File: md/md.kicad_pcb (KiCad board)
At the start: 2 copper layers, 59.7 x 67.3 mm, 55 parts, among them J1 OutB, J2 OutA, J3 Interface, J4 12VJmp, J5 Conn_02x08_Counter_Clockwise, J6 Conn_02x08_Counter_Clockwise, J7 Conn_02x08_Counter_Clockwise, J8 Conn_02x08_Counter_Clockwise, Q1 FETA(IRFB7437PBF), Q2 FETA(IRFB7437PBF), Q3 FETB(IRFB7437PBF), Q4 FETB(IRFB7437PBF), U1 TLP2105, U2 IR7184S, U3 IR7184S, U4 7400, U5 L7812

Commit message: finished working
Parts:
- moved C4 7.62 mm to (179.1, 104.1)
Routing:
- net +24V: track 173.1 -> 174.3 mm
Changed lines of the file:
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@@
     (links 166)
     (no_connects 0)
-    (area 172.644999 50.146665 234.945 134.003335)
+    (area 172.644999 57.074999 232.485001 124.535001)
     (thickness 1.6)
     (drawings 12)
-    (tracks 485)
+    (tracks 488)
     (zones 0)
     (modules 55)
@@
   )
   (module Capacitors_THT:CP_Radial_D8.0mm_P5.00mm (layer F.Cu)
-    (at 179.07 111.76)
+    (at 179.07 104.14)
     (descr "CP, Radial series, Radial, pin pitch=5.00mm, , diameter=8mm, Electrolytic Capacitor")
     (tags "CP Radial series Radial pin pitch 5.00mm  diameter 8mm Electrolytic Capacitor")
@@
   (segment (start 230.505 86.36) (end 230.505 88.15) (width 0.25) (layer F.Cu) (net 2))
   (segment (start 230.505 88.15) (end 230.62 88.265) (width 0.25) (layer F.Cu) (net 2))
+  (segment (start 184.07 104.14) (end 184.07 103.979998) (width 0.25) (layer B.Cu) (net 3))
   (segment (start 189.484 94.488) (end 188.481998 94.488) (width 0.25) (layer F.Cu) (net 3))
   (segment (start 188.481998 94.488) (end 187.719998 95.25) (width 0.25) (layer F.Cu) (net 3))
@@
   (segment (start 212.49 82.37) (end 213.54 83.42) (width 0.6) (layer F.Cu) (net 9))
   (segment (start 213.54 83.42) (end 213.54 83.82) (width 0.6) (layer F.Cu) (net 9))
+  (segment (start 179.07 100.718002) (end 179.07 105.41) (width 2) (layer B.Cu) (net 10))
+  (segment (start 179.07 105.41) (end 179.07 108.96) (width 2) (layer B.Cu) (net 10))
+  (segment (start 179.07 104.14) (end 179.07 105.41) (width 0.25) (layer B.Cu) (net 10))
   (segment (start 213.36 91.96) (end 212.84 91.96) (width 0.6) (layer F.Cu) (net 10))
   (segment (start 212.84 91.96) (end 209.55 95.25) (width 0.6) (layer F.Cu) (net 10))
@@
   (segment (start 185.42 59.549998) (end 185.42 94.368002) (width 2) (layer B.Cu) (net 10))
   (segment (start 185.42 94.368002) (end 179.07 100.718002) (width 2) (layer B.Cu) (net 10))
-  (segment (start 179.07 100.718002) (end 179.07 108.96) (width 2) (layer B.Cu) (net 10))
   (segment (start 179.07 108.96) (end 179.07 111.76) (width 2) (layer B.Cu) (net 10))
   (segment (start 213.36 60.96) (end 210.51 60.96) (width 2) (layer B.Cu) (net 10))
@@
       )
     )
+  )
+  (zone (net 0) (net_name "") (layer B.Mask) (hatch edge 0.508)
+    (connect_pads yes (clearance 0.508))
+    (min_thickness 0.254)
+    (fill yes (arc_segments 16) (thermal_gap 0.508) (thermal_bridge_width 0.508))
+    (polygon
+      (pts
+        (xy 207.01 124.46) (xy 207.01 119.38) (xy 189.23 119.38) (xy 189.23 114.3) (xy 187.96 113.03)
+        (xy 181.61 113.03) (xy 180.34 111.76) (xy 180.34 101.6) (xy 186.69 95.25) (xy 186.69 59.69)
+        (xy 208.28 59.69) (xy 210.82 62.23) (xy 212.09 62.23) (xy 212.09 64.77) (xy 232.41 64.77)
+        (xy 232.41 59.69) (xy 212.09 59.69) (xy 209.55 57.15) (xy 185.42 57.15) (xy 184.15 58.42)
+        (xy 184.15 93.98) (xy 177.8 100.33) (xy 177.8 111.76) (xy 181.61 115.57) (xy 186.69 115.57)
+        (xy 186.69 124.46)
+      )
+    )
+  )
+  (zone (net 0) (net_name "") (layer B.Mask) (hatch edge 0.508)
+    (connect_pads yes (clearance 0.508))
+    (min_thickness 0.254)
+    (fill yes (arc_segments 16) (thermal_gap 0.508) (thermal_bridge_width 0.508))
+    (polygon
+      (pts
+        (xy 212.09 64.77) (xy 203.2 73.66) (xy 203.2 87.63) (xy 205.74 90.17) (xy 207.01 90.17)
+        (xy 208.28 91.44) (xy 208.28 97.79) (xy 207.01 99.06) (xy 205.74 99.06) (xy 205.74 96.52)
+        (xy 203.2 96.52) (xy 203.2 99.06) (xy 205.74 101.6) (xy 208.28 101.6) (xy 209.55 100.33)
+        (xy 212.09 100.33) (xy 213.36 99.06) (xy 215.9 99.06) (xy 215.9 96.52) (xy 210.82 96.52)
+        (xy 210.82 90.17) (xy 208.28 87.63) (xy 205.74 87.63) (xy 205.74 74.93) (xy 214.63 66.04)
+        (xy 214.63 64.77)
+      )
+    )
+  )
+  (zone (net 0) (net_name "") (layer B.Mask) (hatch edge 0.508)
+    (connect_pads yes (clearance 0.508))
+    (min_thickness 0.254)
+    (fill yes (arc_segments 16) (thermal_gap 0.508) (thermal_bridge_width 0.508))
+    (polygon
+      (pts
+        (xy 193.04 99.06) (xy 193.04 96.52) (xy 194.31 95.25) (xy 203.2 95.25) (xy 204.47 95.25)
+        (xy 205.74 96.52) (xy 205.74 99.06) (xy 207.01 99.06) (xy 208.28 97.79) (xy 208.28 95.25)
+        (xy 205.74 92.71) (xy 194.31 92.71) (xy 190.5 96.52) (xy 190.5 99.06)
+      )
+    )
+  )
+  (zone (net 0) (net_name "") (layer B.Mask) (hatch edge 0.508)
+    (connect_pads yes (clearance 0.508))
+    (min_thickness 0.254)
+    (fill yes (arc_segments 16) (thermal_gap 0.508) (thermal_bridge_width 0.508))
+    (polygon
+      (pts
+        (xy 190.5 85.09) (xy 190.5 88.9) (xy 193.04 91.44) (xy 198.12 91.44) (xy 203.2 86.36)
+        (xy 203.2 85.09) (xy 200.66 85.09) (xy 196.85 88.9) (xy 193.04 88.9) (xy 193.04 85.09)
+      )
+    )
+  )
+  (zone (net 0) (net_name "") (layer B.Mask) (hatch edge 0.508)
+    (connect_pads yes (clearance 0.508))
+    (min_thickness 0.254)
+    (fill yes (arc_segments 16) (thermal_gap 0.508) (thermal_bridge_width 0.508))
+    (polygon
+      (pts
+        (xy 207.01 64.77) (xy 207.01 59.69) (xy 186.69 59.69) (xy 186.69 64.77) (xy 194.31 64.77)
+        (xy 194.31 71.12) (xy 187.96 77.47) (xy 187.96 87.63) (xy 186.69 88.9) (xy 186.69 95.25)
+        (xy 185.42 96.52) (xy 185.42 100.33) (xy 186.69 101.6) (xy 201.93 101.6) (xy 204.47 104.14)
+        (xy 210.82 104.14) (xy 213.36 101.6) (xy 217.17 101.6) (xy 218.44 100.33) (xy 218.44 97.79)
+        (xy 218.44 96.52) (xy 215.9 96.52) (xy 215.9 99.06) (xy 213.36 99.06) (xy 212.09 100.33)
+        (xy 209.55 100.33) (xy 208.28 101.6) (xy 205.74 101.6) (xy 203.2 99.06) (xy 187.96 99.06)
+        (xy 187.96 96.52) (xy 189.23 95.25) (xy 189.23 90.17) (xy 190.5 88.9) (xy 190.5 85.09)
+        (xy 190.5 78.74) (xy 196.85 72.39) (xy 196.85 64.77)
+      )
+    )
+  )
+  (zone (net 0) (net_name "") (layer B.Mask) (hatch edge 0.508)
+    (connect_pads yes (clearance 0.508))
+    (min_thickness 0.254)
+    (fill yes (arc_segments 16) (thermal_gap 0.508) (thermal_bridge_width 0.508))
+    (polygon
+      (pts
+        (xy 232.41 124.46) (xy 232.41 119.38) (xy 215.9 119.38) (xy 214.63 118.11) (xy 214.63 107.95)
+        (xy 210.82 104.14) (xy 208.28 104.14) (xy 208.28 105.41) (xy 212.09 109.22) (xy 212.09 124.46)
+      )
+    )
+  )
+  (zone (net 10) (net_name +24V) (layer B.Cu) (hatch edge 0.508)
+    (connect_pads yes (clearance 0.508))
+    (min_thickness 0.254)
+    (fill yes (arc_segments 16) (thermal_gap 0.508) (thermal_bridge_width 0.508))
+    (polygon
+      (pts
+        (xy 212.09 59.69) (xy 212.09 64.77) (xy 232.41 64.77) (xy 232.41 59.69)
+      )
+    )

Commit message: update pcb
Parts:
- removed C11, C8: C, Capacitors_SMD:C_0603
- removed C3: PowerC, Capacitors_THT:C_Disc_D5.0mm_W2.5mm_P5.00mm
- removed PullR(4.7kΩ)1, PullR(4.7kΩ)2: R, Resistors_SMD:R_0603
- removed R13, R14: PullR, Resistors_SMD:R_0603
- added C12: 10uF, Capacitors_SMD:C_1206_HandSoldering, F.Cu at (24.1, 71.8)
- added C13: 10uF, Capacitors_SMD:C_1206_HandSoldering, F.Cu at (15.9, 72.4)
- added J9: PWR_INPUT+, Socket_Strips:Socket_Strip_Straight_2x10_Pitch2.54mm, F.Cu at (41.9, 97.8)
- added JP1: USE_12V, Connectors:GS2, F.Cu at (21.0, 72.4)
- C1: footprint Capacitors_SMD:C_0603 -> Capacitors_SMD:C_0603_HandSoldering
- C10: value RegOutC(1uF) -> 0.1uF; footprint Capacitors_SMD:C_0603 -> Capacitors_SMD:C_0603_HandSoldering
- C2: value BootC(10uF) -> 0.1uF; footprint Capacitors_SMD:C_1206 -> Capacitors_SMD:C_0603_HandSoldering
- C4: value PowerCP -> 0.1uF; footprint Capacitors_THT:CP_Radial_D8.0mm_P5.00mm -> Capacitors_SMD:C_0603_HandSoldering
- C5: value PowerC -> 10uF; footprint Capacitors_THT:C_Disc_D5.0mm_W2.5mm_P5.00mm -> Capacitors_SMD:C_1206_HandSoldering
- C6: value BootC(10uF) -> 10uF; footprint Capacitors_SMD:C_1206 -> Capacitors_SMD:C_1206_HandSoldering
- C7: value 0.1uF -> 470uF; footprint Capacitors_SMD:C_0603 -> Capacitors_THT:CP_Radial_D10.0mm_P5.00mm
- C9: value RegInC(1uF) -> 10uF; footprint Capacitors_SMD:C_0603 -> Capacitors_SMD:C_1206_HandSoldering
- D1, D6: footprint Diodes_SMD:D_SOD-123 -> Diodes_SMD:D_SOD-123F
- D10: value 5VLED(SML-E12P8T86) -> OSYL; footprint LEDs:LED_0603 -> LEDs:LED_0603_HandSoldering
- D11: value 12VLED(SML-E12V8WT86) -> OSHR; footprint LEDs:LED_0603 -> LEDs:LED_0603_HandSoldering
- D2, D3, D4, D5: value RevD(SS2040FL) -> SS2040FL; footprint Diodes_SMD:D_SOD-123 -> Diodes_SMD:D_SOD-123F
- D7: value RegRevC(SS2040FL) -> SS2040FL; footprint Diodes_SMD:D_SOD-123 -> Diodes_SMD:D_SOD-123F
- D8: value DIRLED(SML-E12Y8WT86) -> OSBL; footprint LEDs:LED_0603 -> LEDs:LED_0603_HandSoldering
- D9: value LED(SML-E13BC8TT86) -> OSWT; footprint LEDs:LED_0603 -> LEDs:LED_0603_HandSoldering
- J1: value OutB -> CONTROLL; footprint Wire_Pads:SolderWirePad_single_1-2mmDrill -> Connectors_JST:JST_XH_S04B-XH-A_04x2.50mm_Angled
- J2: value OutA -> OUTA; footprint Wire_Pads:SolderWirePad_single_1-2mmDrill -> Wire_Pads:SolderWirePad_single_1-5mmDrill
- J3: value Interface -> OUTB; footprint Connectors_JST:JST_XH_S04B-XH-A_04x2.50mm_Angled -> Wire_Pads:SolderWirePad_single_1-5mmDrill
- J4: value 12VJmp -> PWR_INPUT+; footprint Connectors:GS2 -> Wire_Pads:SolderWirePad_single_1-5mmDrill
- J5: value Conn_02x08_Counter_Clockwise -> PWR_INPUT-; footprint Socket_Strips:Socket_Strip_Straight_2x08_Pitch2.54mm -> Wire_Pads:SolderWirePad_single_1-5mmDrill
- J6, J7, J8: value Conn_02x08_Counter_Clockwise -> PWR_INPUT+; footprint Socket_Strips:Socket_Strip_Straight_2x08_Pitch2.54mm -> Socket_Strips:Socket_Strip_Straight_2x10_Pitch2.54mm
- Q1, Q2: value FETA(IRFB7437PBF) -> IRFB7437PBF; footprint TO_SOT_Packages_THT:TO-220-3_Horizontal_Reversed -> TO_SOT_Packages_THT:TO-220-3_Horizontal
- Q3, Q4: value FETB(IRFB7437PBF) -> IRFB7437PBF; footprint TO_SOT_Packages_THT:TO-220-3_Horizontal_Reversed -> TO_SOT_Packages_THT:TO-220-3_Horizontal
- R1: value TLP_R(470Ω) -> 10Ω; footprint Resistors_SMD:R_0603 -> Resistors_SMD:R_1206_HandSoldering
- R10: value TLP_R(470Ω) -> 470Ω; footprint Resistors_SMD:R_0603 -> Resistors_SMD:R_0603_HandSoldering
- R11: value 5VLEDR(470Ω) -> 220Ω; footprint Resistors_SMD:R_0603 -> Resistors_SMD:R_0603_HandSoldering
- R12: value 12VLEDR(1.2kΩ) -> 220Ω; footprint Resistors_SMD:R_0603 -> Resistors_SMD:R_0603_HandSoldering
- R2, R8: value GateR(8.2Ω) -> 10Ω; footprint Resistors_SMD:R_1206 -> Resistors_SMD:R_1206_HandSoldering
- R3: value GateR(8.2Ω) -> 4.7kΩ; footprint Resistors_SMD:R_1206 -> Resistors_SMD:R_0603_HandSoldering
- R4, R5: value PullR(4.7kΩ) -> 4.7kΩ; footprint Resistors_SMD:R_0603 -> Resistors_SMD:R_0603_HandSoldering
- R6: value DIRLEDR(470Ω) -> 4.7kΩ; footprint Resistors_SMD:R_0603 -> Resistors_SMD:R_0603_HandSoldering
- R7: value PWMLEDR(470Ω) -> 10Ω; footprint Resistors_SMD:R_0603 -> Resistors_SMD:R_1206_HandSoldering
- R9: value GateR(8.2Ω) -> 150Ω; footprint Resistors_SMD:R_1206 -> Resistors_SMD:R_0603_HandSoldering
- U1: value TLP2105 -> 74HC00; footprint SMD_Packages:SOIC-8-N -> SMD_Packages:SOIC-14_N
- U2: value IR7184S -> TLP2105
- U4: value 7400 -> IR7184S; footprint SMD_Packages:SOIC-14_N -> SMD_Packages:SOIC-8-N
- U5: value L7812 -> LM7812_TO220; footprint TO_SOT_Packages_THT:TO-220-3_Horizontal_Reversed -> TO_SOT_Packages_THT:TO-220-3_Horizontal
- moved C7 211.3 mm to (20.3, 66.0)
- moved C6 206.1 mm to (24.1, 78.7), turned to 270 degrees
- moved J4 203.1 mm to (17.8, 50.8), turned to 0 degrees
- moved J8 200.7 mm to (14.0, 97.8)
- moved U5 195.7 mm to (20.3, 74.9), turned to 180 degrees
- moved J5 195.6 mm to (17.8, 57.1), turned to 0 degrees
- moved D7 193.2 mm to (24.1, 85.1), turned to 270 degrees
- moved J6 191.5 mm to (14.0, 40.6)
- moved J3 186.7 mm to (36.8, 72.4), turned to 0 degrees
- moved U3 184.0 mm to (51.4, 52.7), turned to 0 degrees
- moved D6 183.1 mm to (49.9, 81.3)
- moved Q1 182.7 mm to (25.4, 66.0), turned to 0 degrees
- moved R3 179.4 mm to (34.3, 59.7), turned to 90 degrees
- moved R1 178.9 mm to (49.5, 60.3), turned to 0 degrees
- moved D4 178.0 mm to (29.2, 72.4), turned to 180 degrees
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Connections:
- C1 pad 1: +12V -> GND
- C1 pad 2: GNDPWR -> +5V
- C10 pad 1: +12V -> GNDPWR
- C10 pad 2: GNDPWR -> +12V
- C2 pad 1: Net-(C2-Pad1) -> GND
- C2 pad 2: Net-(C2-Pad2) -> +12V
- C4 pad 1: +24V -> GNDPWR
- C4 pad 2: GNDPWR -> +12V
- C5 pad 1: +24V -> Net-(C5-Pad1)
- C5 pad 2: GNDPWR -> Net-(C5-Pad2)
- C6 pad 1: Net-(C6-Pad1) -> +24V
- C6 pad 2: Net-(C6-Pad2) -> GNDPWR
- C7 pad 1: +12V -> +24V
- C9 pad 1: +24V -> Net-(C9-Pad1)
- C9 pad 2: GNDPWR -> Net-(C9-Pad2)
- D1 pad 1: Net-(C2-Pad1) -> Net-(C5-Pad1)
- D10 pad 1: GNDPWR -> GND
- D11 pad 1: GNDPWR -> GND
- D2 pad 2: Net-(C2-Pad2) -> Net-(C5-Pad2)
- D3 pad 1: Net-(C2-Pad2) -> Net-(C5-Pad2)
- D4 pad 2: Net-(C6-Pad2) -> Net-(C9-Pad2)
- D5 pad 1: Net-(C6-Pad2) -> Net-(C9-Pad2)
- D6 pad 1: Net-(C6-Pad1) -> Net-(C9-Pad1)
- D9 pad 1: GND -> GNDPWR
- J1 pad 1: Net-(C2-Pad2) -> +5V
- J2 pad 1: Net-(C6-Pad2) -> Net-(C5-Pad2)
- J3 pad 1: GND -> Net-(C9-Pad2)
- J5 pad 1: +24V -> GNDPWR
- J7 pad 1: GNDPWR -> +24V
- J7 pad 10: GNDPWR -> +24V
- J7 pad 11: GNDPWR -> +24V
- J7 pad 12: GNDPWR -> +24V
- J7 pad 13: GNDPWR -> +24V
- J7 pad 14: GNDPWR -> +24V
- J7 pad 15: GNDPWR -> +24V
- J7 pad 16: GNDPWR -> +24V
- J7 pad 2: GNDPWR -> +24V
- J7 pad 3: GNDPWR -> +24V
- J7 pad 4: GNDPWR -> +24V
- J7 pad 5: GNDPWR -> +24V
- J7 pad 6: GNDPWR -> +24V
- J7 pad 7: GNDPWR -> +24V
- J7 pad 8: GNDPWR -> +24V
- J7 pad 9: GNDPWR -> +24V
- Q1 pad 3: Net-(C2-Pad2) -> Net-(C5-Pad2)
- Q2 pad 2: Net-(C2-Pad2) -> Net-(C5-Pad2)
- Q3 pad 1: Net-(PullR(4.7kΩ)1-Pad1) -> Net-(Q3-Pad1)
- Q3 pad 3: Net-(C6-Pad2) -> Net-(C9-Pad2)
- Q4 pad 1: Net-(PullR(4.7kΩ)2-Pad1) -> Net-(Q4-Pad1)
- Q4 pad 2: Net-(C6-Pad2) -> Net-(C9-Pad2)
- R1 pad 1: Net-(R1-Pad1) -> Net-(Q1-Pad1)
- R1 pad 2: +5V -> Net-(R1-Pad2)
- R10 pad 1: Net-(R10-Pad1) -> +12V
- R10 pad 2: +5V -> Net-(D9-Pad2)
- R11 pad 1: +5V -> /DIR
- R12 pad 1: +12V -> /PWM
- R2 pad 1: Net-(Q1-Pad1) -> Net-(Q2-Pad1)
- R3 pad 1: Net-(Q2-Pad1) -> Net-(C5-Pad2)
- R3 pad 2: Net-(R3-Pad2) -> Net-(Q1-Pad1)
- R4 pad 1: Net-(Q1-Pad1) -> Net-(Q2-Pad1)
- R4 pad 2: Net-(C2-Pad2) -> GNDPWR
- R5 pad 1: Net-(Q2-Pad1) -> Net-(C9-Pad2)
- R5 pad 2: GNDPWR -> Net-(Q3-Pad1)
- R6 pad 1: /DIR -> Net-(Q4-Pad1)
- R6 pad 2: Net-(D8-Pad2) -> GNDPWR
- R7 pad 1: /PWM -> Net-(Q3-Pad1)
- R7 pad 2: Net-(D9-Pad2) -> Net-(R7-Pad2)
- R8 pad 1: Net-(PullR(4.7kΩ)1-Pad1) -> Net-(Q4-Pad1)
- R9 pad 1: Net-(PullR(4.7kΩ)2-Pad1) -> +5V
- R9 pad 2: Net-(R9-Pad2) -> Net-(D8-Pad2)
- U1 pad 1: Net-(R1-Pad1) -> (no net)
- U1 pad 2: Net-(U1-Pad2) -> (no net)
- U1 pad 3: Net-(R10-Pad1) -> (no net)
- U1 pad 4: Net-(U1-Pad4) -> /DIR
- U1 pad 5: GNDPWR -> /DIR
- U1 pad 6: /OUTB -> Net-(U1-Pad6)
- U1 pad 7: /OUTA -> GND
- U1 pad 8: +12V -> (no net)
- U2 pad 1: +12V -> /PWM
- U2 pad 2: /OUTA -> /DIR
- U2 pad 3: Net-(R13-Pad1) -> /PWM
- U2 pad 4: GNDPWR -> Net-(U1-Pad6)
- U2 pad 5: Net-(R2-Pad2) -> GNDPWR
- U2 pad 6: Net-(C2-Pad2) -> /OUTB
- U2 pad 7: Net-(R3-Pad2) -> /OUTA
- U2 pad 8: Net-(C2-Pad1) -> +12V
- U3 pad 2: /OUTB -> /OUTA
- U3 pad 3: Net-(R14-Pad2) -> +12V
- U3 pad 5: Net-(R8-Pad2) -> Net-(R2-Pad2)
- U3 pad 6: Net-(C6-Pad2) -> Net-(C5-Pad2)
- U3 pad 7: Net-(R9-Pad2) -> Net-(R1-Pad2)
- U3 pad 8: Net-(C6-Pad1) -> Net-(C5-Pad1)
- U4 pad 1: /DIR -> +12V
- U4 pad 2: /DIR -> /OUTB
- U4 pad 3: Net-(U4-Pad12) -> +12V
- U4 pad 4: Net-(U4-Pad4) -> GNDPWR
- U4 pad 5: Net-(U4-Pad5) -> Net-(R8-Pad2)
- U4 pad 6: Net-(U4-Pad6) -> Net-(C9-Pad2)
- U4 pad 7: GND -> Net-(R7-Pad2)
- U4 pad 8: Net-(U1-Pad2) -> Net-(C9-Pad1)
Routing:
- net Net-(C6-Pad2): track 88.0 -> 0.00 mm
- net +24V: track 174.3 -> 99.6 mm
- net +12V: track 72.9 -> 141.1 mm
- net Net-(C2-Pad2): track 60.8 -> 0.00 mm
- net Net-(C5-Pad2): track 0.00 -> 57.6 mm, vias 0 -> 2
- net Net-(C9-Pad2): track 0.00 -> 54.0 mm, vias 0 -> 1
- net Net-(PullR(4.7kΩ)2-Pad1): track 39.8 -> 0.00 mm
- net GND: track 22.3 -> 56.1 mm
- net Net-(Q4-Pad1): track 0.00 -> 33.5 mm, vias 0 -> 2
- net Net-(PullR(4.7kΩ)1-Pad1): track 30.3 -> 0.00 mm
- net Net-(Q1-Pad1): track 11.7 -> 38.6 mm
- net Net-(Q3-Pad1): track 0.00 -> 26.5 mm
- net Net-(R3-Pad2): track 20.9 -> 0.00 mm
- net Net-(R9-Pad2): track 13.6 -> 0.00 mm
- net Net-(R1-Pad2): track 0.00 -> 13.6 mm
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- added copper zone on B.Cu, net +12V
- removed copper zone on B.Cu, net +24V
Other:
- board size 59.7 x 67.3 mm -> 54.6 x 62.2 mm

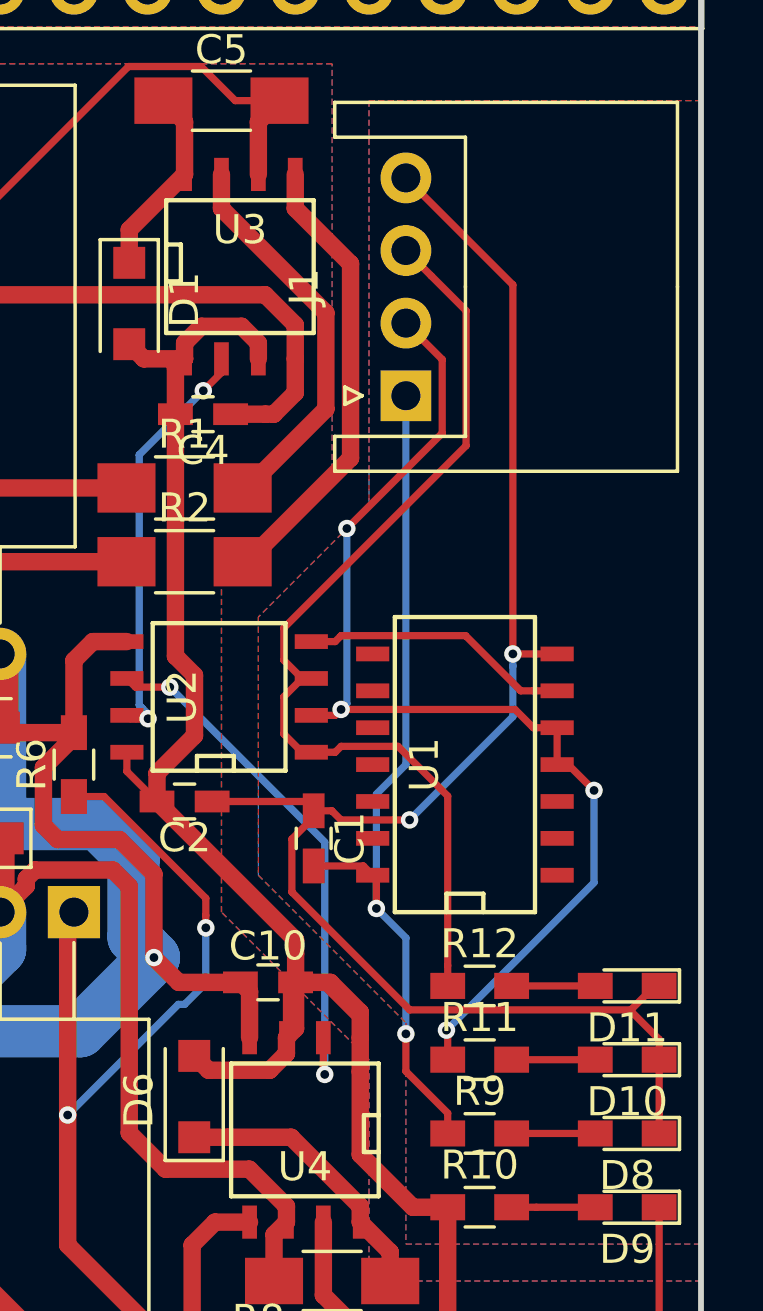
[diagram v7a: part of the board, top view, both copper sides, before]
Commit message: add current limit regisiter for TLP2105
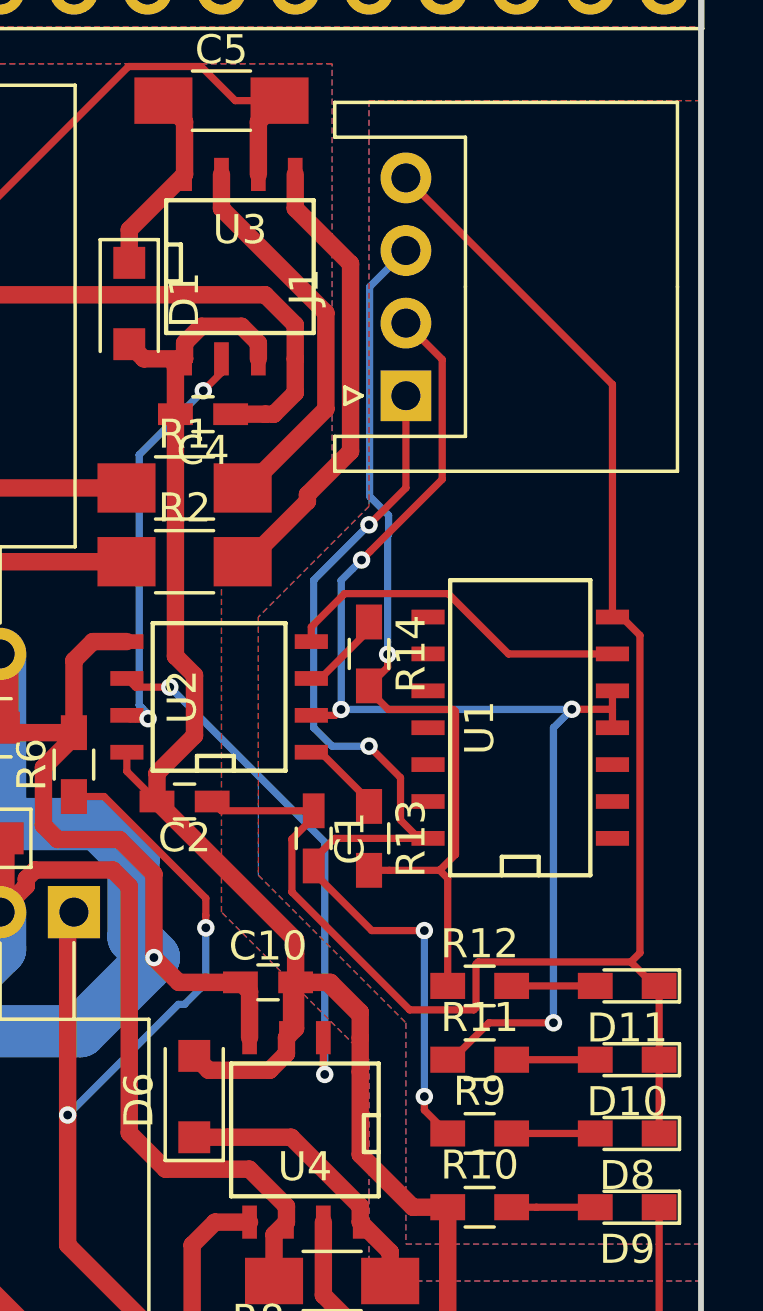
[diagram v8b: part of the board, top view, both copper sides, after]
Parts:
- added R13: 330Ω, Resistors_SMD:R_0603_HandSoldering, F.Cu at (55.9, 72.4)
- added R14: 330Ω, Resistors_SMD:R_0603_HandSoldering, F.Cu at (55.9, 66.0)
- moved U1 2.29 mm to (61.0, 68.6)
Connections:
- U2 pad 1: /PWM -> Net-(R13-Pad1)
- U2 pad 3: /PWM -> Net-(R14-Pad1)
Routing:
- net +5V: track 30.2 -> 35.8 mm, vias 2 -> 4
- net /DIR: track 38.4 -> 42.2 mm
- net Net-(R14-Pad1): track 0.00 -> 2.95 mm
- net Net-(R13-Pad1): track 0.00 -> 2.87 mm
- net Net-(U1-Pad6): track 9.33 -> 12.2 mm
- net GND: track 56.1 -> 58.7 mm, vias 2 -> 0
- net /PWM: track 34.2 -> 31.7 mm, vias 0 -> 1
